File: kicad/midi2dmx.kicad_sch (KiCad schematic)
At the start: 29 parts, among them IC1 MAX485E, P1 MIDI Input, P2 MIDI Through, P3 DMX Out, P4 9V Power, SW1 SW_LED_blue, U1 ProMini

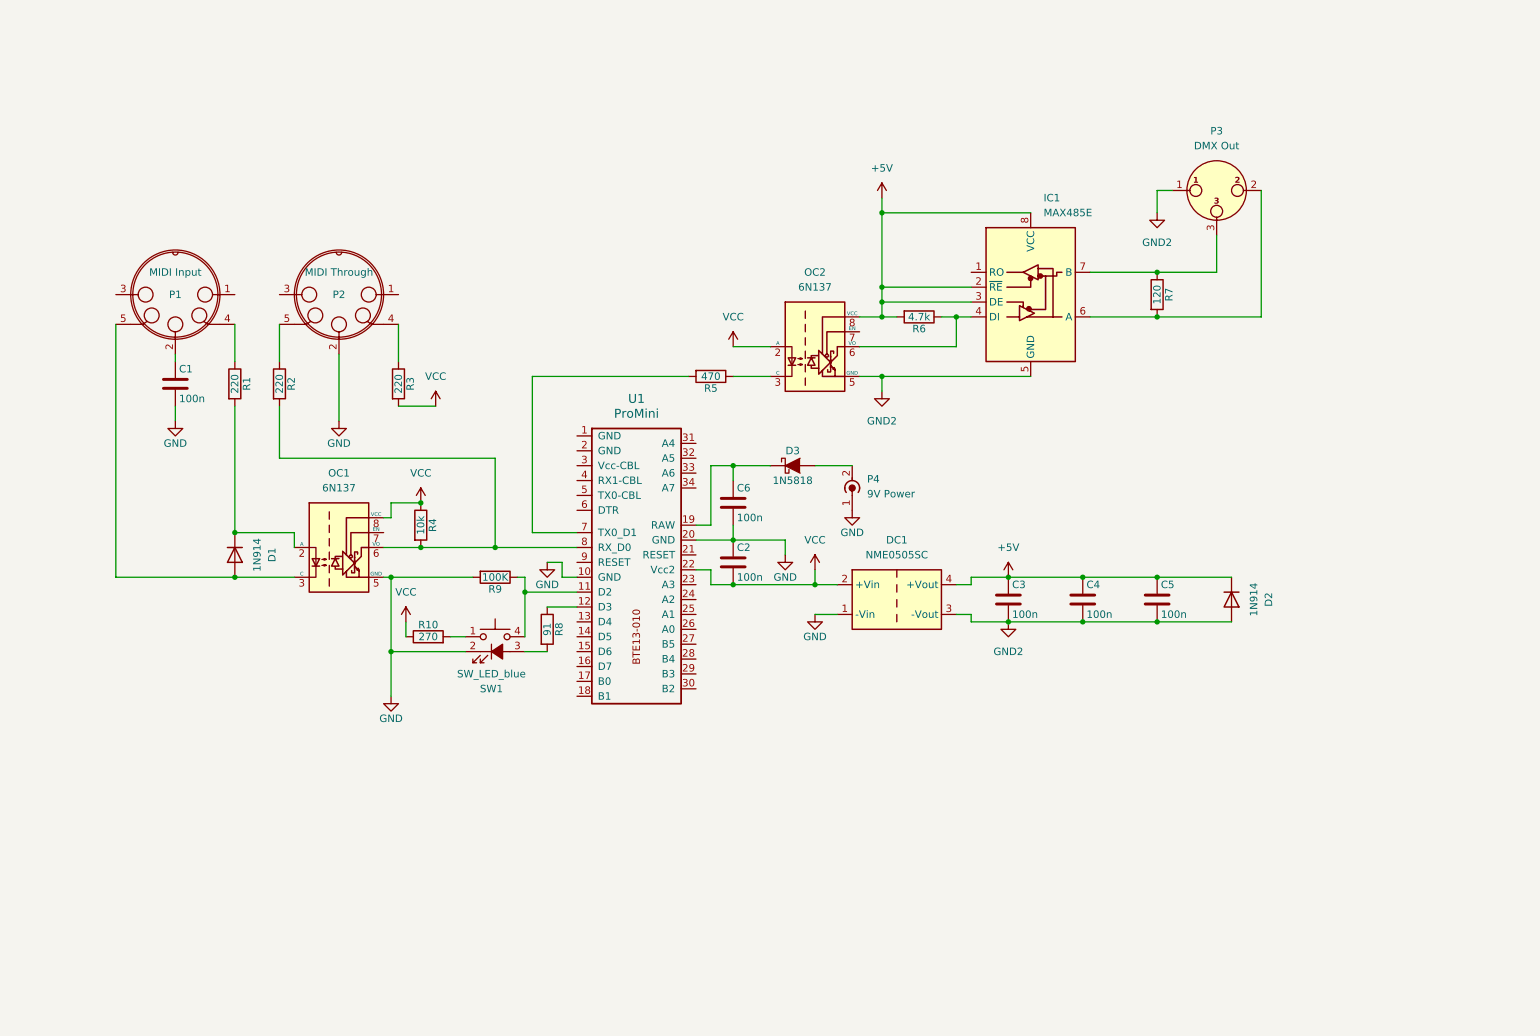
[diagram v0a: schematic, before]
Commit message: update schematic
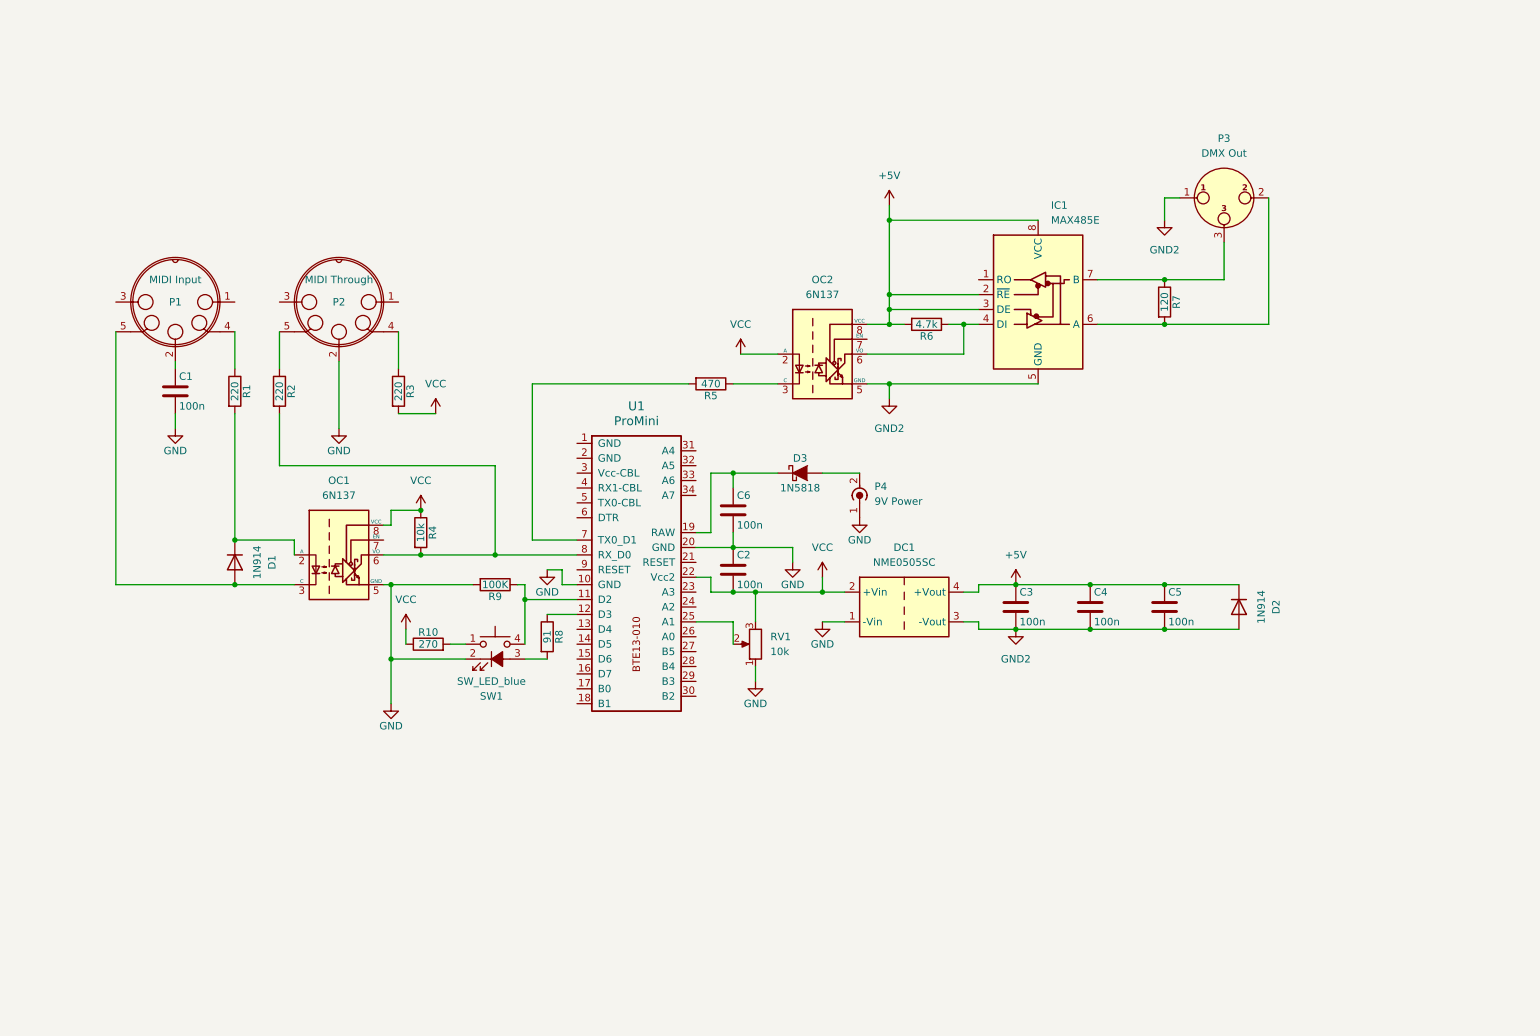
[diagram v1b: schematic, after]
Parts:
- added RV1: 10k, Connector_Molex:Molex_KK-254_AE-6410-03A_1x03_P2.54mm_Vertical, symbol Device:R_Potentiometer
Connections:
- net GND: now also RV1.1
- net VCC: now also RV1.3
- net at U1.25 (A1): now also RV1.2
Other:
- moved on the sheet: C1, C2, C3, C4, C5, C6, D1, D2, D3, DC1, IC1, OC1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

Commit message: update schematic
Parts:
- RV1: URL (none) -> https://www.reichelt.de/drehpotentiometer-10-kohm-6-mm-line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
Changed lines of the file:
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@@
       (effects (font (size 1.27 1.27)) hide)
     )
-    (property "Datasheet" "~" (at 147.32 128.27 0)
+    (property "Datasheet" "https://cdn-reichelt.de/documents/datenblatt/B300/P231_ENG_TDS.pdf" (at 147.32 128.27 0)
       (effects (font (size 1.27 1.27)) hide)
     )
+    (property "URL" "https://www.reichelt.de/drehpotentiometer-10-kohm-6-mm-linear-bi-p231-fd20br-p238719.html?&trstct=pol_14&nbc=1" (at 147.32 128.27 0)
+      (effects (font (size 1.27 1.27)) hide)
+    )

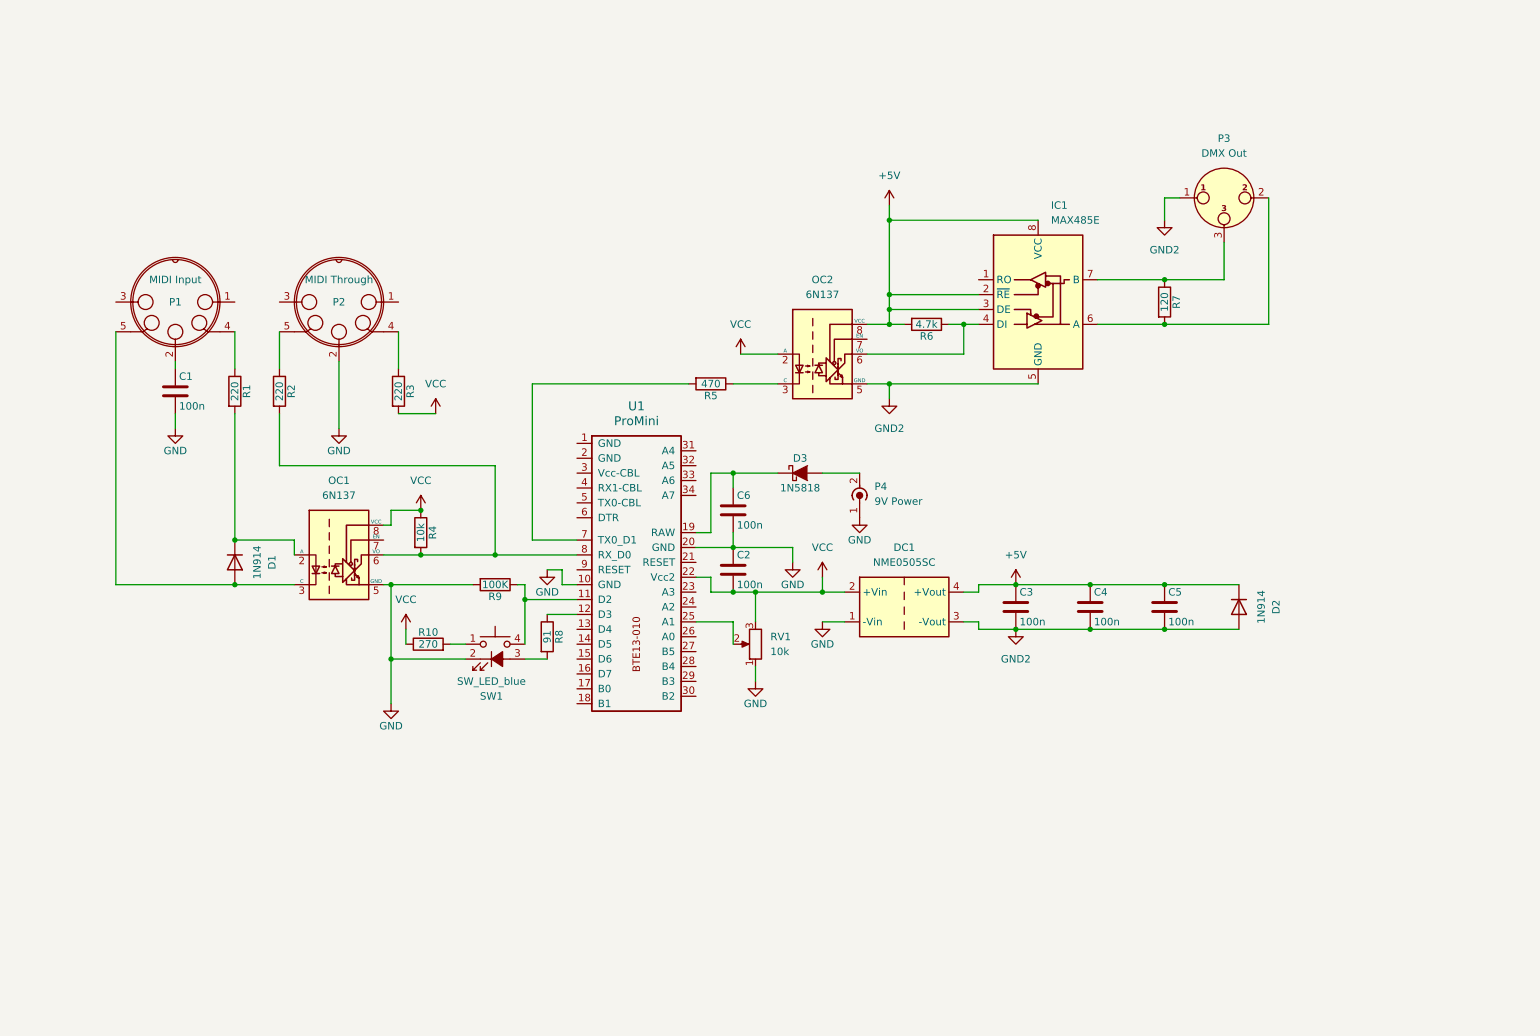
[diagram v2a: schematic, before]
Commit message: rework PCB to use SMD
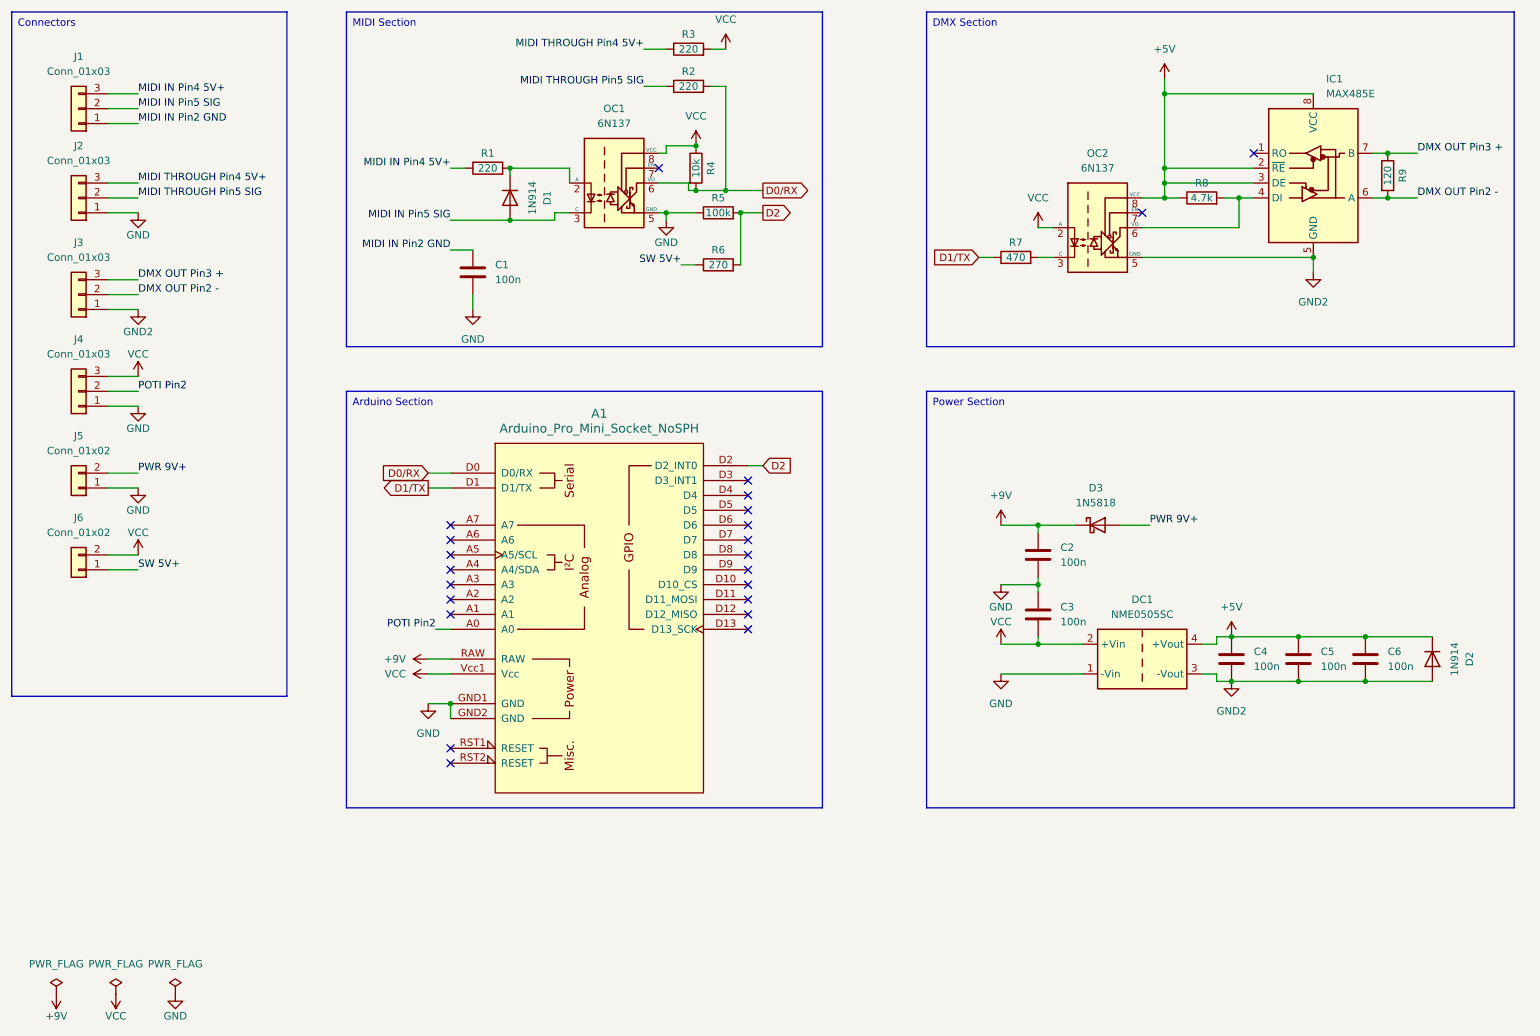
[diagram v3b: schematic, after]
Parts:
- removed C1, C2, C3, C4, C5, C6: 100n, Capacitor_THT:C_Disc_D5.0mm_W2.5mm_P2.50mm, symbol midiextender-rescue:C
- removed D3: 1N5818, Diode_THT:D_DO-34_SOD68_P7.62mm_Horizontal, symbol midiextender-rescue:D_Schottky
- removed P1: MIDI Input, Connector_Molex:Molex_KK-254_AE-6410-03A_1x03_P2.54mm_Vertical, symbol midiextender-rescue:DIN_5
- removed P2: MIDI Through, Connector_Molex:Molex_KK-254_AE-6410-03A_1x03_P2.54mm_Vertical, symbol midiextender-rescue:DIN_5
- removed P3: DMX Out, Connector_Molex:Molex_KK-254_AE-6410-03A_1x03_P2.54mm_Vertical, symbol Connector_Audio:XLR3
- removed P4: 9V Power, Connector_Molex:Molex_KK-254_AE-6410-02A_1x02_P2.54mm_Vertical, symbol Connector:Conn_Coaxial_Power
- removed R1, R2, R3: 220, Resistor_THT:R_Axial_DIN0207_L6.3mm_D2.5mm_P7.62mm_Horizontal, symbol midiextender-rescue:R
- removed R10: 270, Resistor_THT:R_Axial_DIN0207_L6.3mm_D2.5mm_P7.62mm_Horizontal, symbol midiextender-rescue:R
- removed R4: 10k, Resistor_THT:R_Axial_DIN0207_L6.3mm_D2.5mm_P7.62mm_Horizontal, symbol midiextender-rescue:R
- removed R5: 470, Resistor_THT:R_Axial_DIN0207_L6.3mm_D2.5mm_P7.62mm_Horizontal, symbol midiextender-rescue:R
- removed R6: 4.7k, Resistor_THT:R_Axial_DIN0207_L6.3mm_D2.5mm_P7.62mm_Horizontal, symbol midiextender-rescue:R
- removed R7: 120, Resistor_THT:R_Axial_DIN0207_L6.3mm_D2.5mm_P7.62mm_Horizontal, symbol midiextender-rescue:R
- removed R8: 91, Resistor_THT:R_Axial_DIN0207_L6.3mm_D2.5mm_P7.62mm_Horizontal, symbol midiextender-rescue:R
- removed R9: 100K, Resistor_THT:R_Axial_DIN0207_L6.3mm_D2.5mm_P7.62mm_Horizontal, symbol midiextender-rescue:R
- removed RV1: 10k, Connector_Molex:Molex_KK-254_AE-6410-03A_1x03_P2.54mm_Vertical, symbol Device:R_Potentiometer
- removed SW1: SW_LED_blue, Connector_Molex:Molex_KK-254_AE-6410-04A_1x04_P2.54mm_Vertical, symbol Switch:SW_MEC_5G_LED
- removed U1: ProMini, Arduino-clone:ABK-PRO-MINI, symbol j_ProcessorBoards:ProMini
- added A1: Arduino_Pro_Mini_Socket_NoSPH, PCM_arduino-library:Arduino_Pro_Mini_Socket_NoSPH, symbol PCM_arduino-library:Arduino_Pro_Mini_Socket_NoSPH
- added C1, C2, C3, C4, C5, C6: 100n, Capacitor_SMD:C_1206_3216Metric, symbol Device:C
- added D3: 1N5818, Diode_SMD:D_1206_3216Metric, symbol Device:D_Schottky
- added J1, J2, J3, J4: Conn_01x03, Connector_Molex:Molex_KK-254_AE-6410-03A_1x03_P2.54mm_Vertical, symbol Connector_Generic:Conn_01x03
- added J5, J6: Conn_01x02, Connector_Molex:Molex_KK-254_AE-6410-02A_1x02_P2.54mm_Vertical, symbol Connector_Generic:Conn_01x02
- added R1, R2, R3: 220, Resistor_SMD:R_1206_3216Metric, symbol Device:R
- added R4: 10k, Resistor_SMD:R_1206_3216Metric, symbol Device:R
- added R5: 100k, Resistor_SMD:R_1206_3216Metric, symbol Device:R
- added R6: 270, Resistor_SMD:R_1206_3216Metric, symbol Device:R
- added R7: 470, Resistor_SMD:R_1206_3216Metric, symbol Device:R
- added R8: 4.7k, Resistor_SMD:R_1206_3216Metric, symbol Device:R
- added R9: 120, Resistor_SMD:R_1206_3216Metric, symbol Device:R
- D1, D2: footprint Diode_THT:D_DO-35_SOD27_P7.62mm_Horizontal -> Diode_SMD:D_1206_3216Metric
- IC1, OC1, OC2: footprint Package_DIP:DIP-8_W7.62mm -> Package_DIP:SMDIP-8_W7.62mm
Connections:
- net +5V: now also C4.1, C5.1, C6.1, R8.1
- net GND: now also A1.GND1 (GND), A1.GND2 (GND), C1.2, C2.2, C3.1, J2.1 (Pin_1), J4.1 (Pin_1), J5.1 (Pin_1), R5.1
- net GND2: now also C4.2, C5.2, C6.2, J3.1 (Pin_1)
- net VCC: now also A1.Vcc1 (Vcc), C3.2, J4.3 (Pin_3), J6.2 (Pin_2), R3.2, R4.1
- net D0/RX: now reaches OC1.6 (VO)
- net D0/RX: now also A1.D0 (D0/RX), R2.2, R4.2
- net at IC1.4 (DI), OC2.6 (VO): now also R8.2
- net DMX OUT Pin2 -: now reaches IC1.6 (A)
- net DMX OUT Pin2 -: now also J3.2 (Pin_2), R9.2
- net DMX OUT Pin3 +: now reaches IC1.7 (B)
- net DMX OUT Pin3 +: now also J3.3 (Pin_3), R9.1
- net at OC2.3 (C): now also R7.2
- net at D1.1 (K), OC1.2 (A): now also R1.2
- net MIDI IN Pin5 SIG: now reaches D1.2 (A), OC1.3 (C)
- net MIDI IN Pin5 SIG: now also J1.2 (Pin_2)
- new net +9V: A1.RAW, C2.1, D3.1 (K)
- new net D1/TX: A1.D1 (D1/TX), R7.1
- new net D2: A1.D2 (D2_INT0), R5.2, R6.2
- new net MIDI IN Pin2 GND: C1.1, J1.1 (Pin_1)
- new net MIDI IN Pin4 5V+: J1.3 (Pin_3), R1.1
- new net MIDI THROUGH Pin4 5V+: J2.3 (Pin_3), R3.1
- new net MIDI THROUGH Pin5 SIG: J2.2 (Pin_2), R2.1
- new net POTI Pin2: A1.A0, J4.2 (Pin_2)
- new net PWR 9V+: D3.2 (A), J5.2 (Pin_2)
- new net SW 5V+: J6.1 (Pin_1), R6.1
- no-connect marks 0 -> 23
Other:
- moved on the sheet: D1, D2, DC1, IC1, OC1, OC2
